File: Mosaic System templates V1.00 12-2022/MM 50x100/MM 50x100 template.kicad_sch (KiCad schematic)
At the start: 21 parts, among them J1 Conn_01x04, J2 INPUT, J3 CLK_INPUT, J4 OUTPUT, SW1 SPDT, SW2 SPST, U1 Opamp_Dual

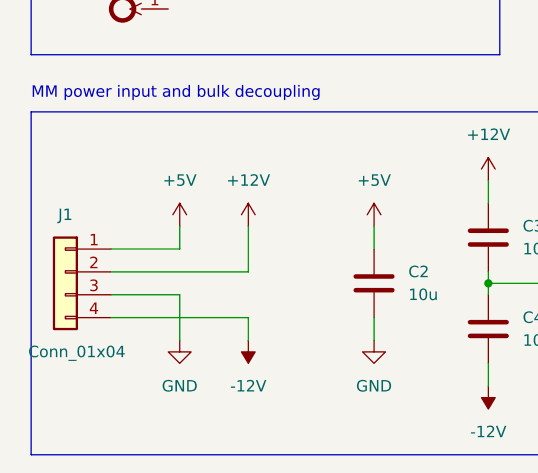
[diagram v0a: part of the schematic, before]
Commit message: V1.1
Clean up of some redundant footprints and added the correct polygons for the keepout area of the corners.
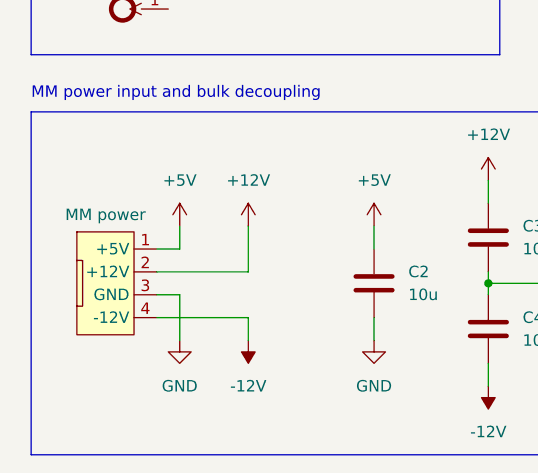
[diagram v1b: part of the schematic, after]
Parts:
- removed J1: Conn_01x04, 0-MM:JST_B4B-PH-SM4-TB_LF_SN_0, symbol Connector_Generic:Conn_01x04
- added J1: MM power, symbol 0-MM:MM power
- C2, C3, C4, C5: footprint Capacitor_SMD:C_0805_2012Metric -> (none)
- D2: footprint 0-MM:LED 0805 reverse mount -> (none)
- SW2: footprint 0-MM:12X12MM_THT_TACT -> (none)
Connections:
- net +12V: now also J1.2 (+12V)
- net +5V: now also J1.1 (+5V)
- net -12V: now also J1.4 (-12V)
- net GND: now also J1.3 (GND)
